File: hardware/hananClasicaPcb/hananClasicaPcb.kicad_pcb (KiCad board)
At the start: 2 copper layers, 77 x 92 mm, 32 parts, among them J1 Jack-DC, J2 Conn_02x04_Top_Bottom, U1 MCP4901

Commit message: hananClasicaPcb v2.0: J2 header -> columna de pads arcade compacta (ODS), gerber regenerado
Co-Authored-By: Claude Fable 5.1 <noreply@anthropic.com>
Claude-Session: https://claude.ai/code/session_018KSRbDX7mTqiibDixEKAXu
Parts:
- J2: value Conn_02x04_Top_Bottom -> Hanan_PadsArcade_1x08_Pares_Compacto; footprint Connector_PinHeader_2.00mm:PinHeader_1x08_P2.00mm_Vertical -> ODS:Hanan_PadsArcade_1x08_Pares_Compacto
- moved J2 10.6 mm to (120.7, 102.0)
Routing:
- net Net-(J2-Pad8): track 153.9 -> 135.8 mm
- net GND: track 440.9 -> 453.4 mm
- net Net-(J2-Pad5): track 144.3 -> 134.6 mm
- net Net-(J2-Pad1): track 136.9 -> 144.1 mm
- net Net-(J2-Pad4): track 128.7 -> 130.8 mm

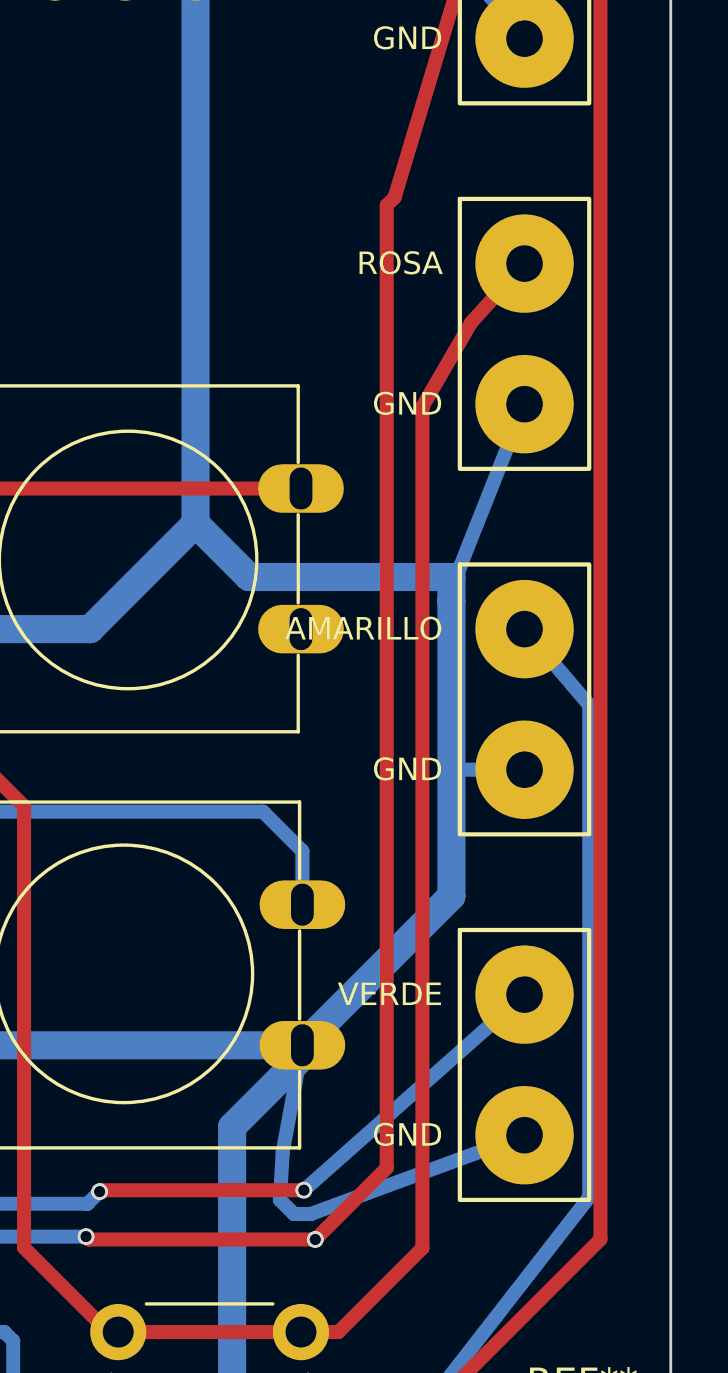
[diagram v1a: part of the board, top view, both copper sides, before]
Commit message: hananClasicaPcb v2.0: columna de pads arcade con grupos espejados; gerber regenerado
Co-Authored-By: Claude Fable 5.1 <noreply@anthropic.com>
Claude-Session: https://claude.ai/code/session_018KSRbDX7mTqiibDixEKAXu
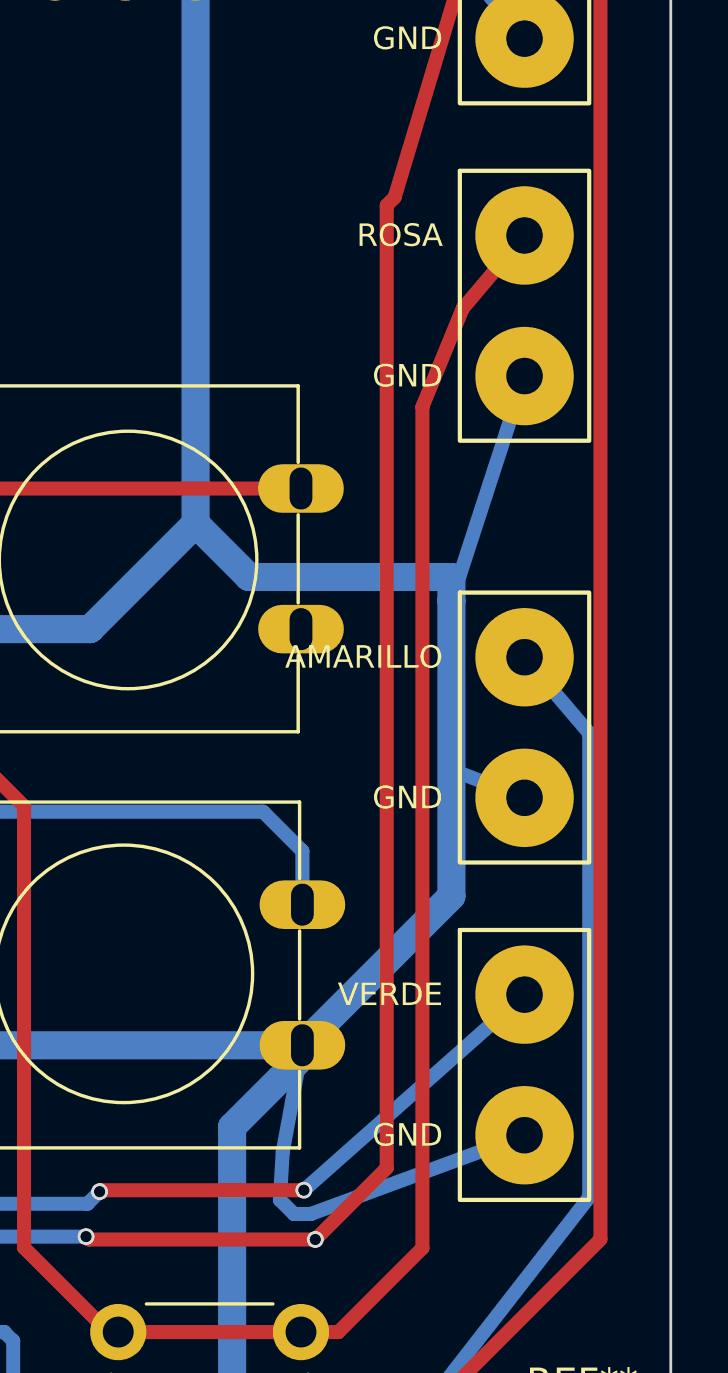
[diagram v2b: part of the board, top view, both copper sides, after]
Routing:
- net GND: track 453.4 -> 454.5 mm
- net Net-(J2-Pad5): track 134.6 -> 133.6 mm
- net Net-(J2-Pad4): track 130.8 -> 131.7 mm
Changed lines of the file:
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@@
 		(layer "F.Cu")
 		(at 120.7 102)
-		(descr "Hanan Cumbia (clasica, version compacta): 8 pads para soldar los cables de los 4 botones arcade, en UNA columna, agrupados de a pares (senal arriba, GND abajo): 5 mm dentro del par; pares 1-2 arriba (paso 17, el LED D1 en el hueco) y pares 3-4 ESPEJADOS respecto del centro de la placa 150x75 (a 4.6 mm de cada borde); offsets 0/5, 13/18, 26/31, 39/44 (version COMPACTA, 44 mm, para la Hanan clasica 77x92 donde la de 66 mm no entra; mismo orden/numeracion/colores). Pad redondo 3.5 mm, agujero 1.3 mm (cable 22 AWG). NUMERACION = pines del simbolo J2 Conn_02x04_Top_Bottom del esquematico hananMiniPcb, en el MISMO orden de colores que el header original: slot1=pad1 (D3, BLANCO/cencerro) slot2=pad2 GND, slot3=pad4 (D8, ROSA/conga) slot4=pad3 GND, slot5=pad5 (D4, AMARILLO/kick) slot6=pad6 GND, slot7=pad8 (D7, VERDE/guiro) slot8=pad7 GND. Colores = botones del panel Mini (manual + firmware hanan26Taller, 2026-10-07). ORIGEN = centro del pad del slot 1 (arriba).")
+		(descr "Hanan Cumbia (clasica, version compacta): 8 pads para soldar los cables de los 4 botones arcade, en UNA columna, agrupados de a pares (senal arriba, GND abajo): 5 mm dentro del par; pares 1-2 arriba (paso 17, el LED D1 en el hueco) y pares 3-4 ESPEJADOS respecto del centro de la placa 150x75 (a 4.6 mm de cada borde); offsets 0/5, 12/17, 27/32, 39/44 (grupos 1-2 y 3-4 ESPEJADOS respecto del centro y=22) (version COMPACTA, 44 mm, para la Hanan clasica 77x92 donde la de 66 mm no entra; mismo orden/numeracion/colores). Pad redondo 3.5 mm, agujero 1.3 mm (cable 22 AWG). NUMERACION = pines del simbolo J2 Conn_02x04_Top_Bottom del esquematico hananMiniPcb, en el MISMO orden de colores que el header original: slot1=pad1 (D3, BLANCO/cencerro) slot2=pad2 GND, slot3=pad4 (D8, ROSA/conga) slot4=pad3 GND, slot5=pad5 (D4, AMARILLO/kick) slot6=pad6 GND, slot7=pad8 (D7, VERDE/guiro) slot8=pad7 GND. Colores = botones del panel Mini (manual + firmware hanan26Taller, 2026-10-07). ORIGEN = centro del pad del slot 1 (arriba).")
 		(tags "hanan arcade solder pads wire pads cable THT 1x08 pares")
 		(property "Reference" "J2"
@@
 		)
 		(fp_rect
-			(start -2.3 10.7)
-			(end 2.3 20.3)
+			(start -2.3 9.7)
+			(end 2.3 19.3)
 			(stroke
 				(width 0.15)
@@
 		)
 		(fp_rect
-			(start -2.3 23.7)
-			(end 2.3 33.3)
+			(start -2.3 24.7)
+			(end 2.3 34.3)
 			(stroke
 				(width 0.15)
@@
 		)
 		(fp_rect
-			(start -2.3 10.7)
-			(end 2.3 20.3)
+			(start -2.3 9.7)
+			(end 2.3 19.3)
 			(stroke
 				(width 0.15)
@@
 		)
 		(fp_rect
-			(start -2.3 23.7)
-			(end 2.3 33.3)
+			(start -2.3 24.7)
+			(end 2.3 34.3)
 			(stroke
 				(width 0.15)
@@
 		)
 		(fp_rect
-			(start -2.5 10.5)
-			(end 2.5 20.5)
+			(start -2.5 9.5)
+			(end 2.5 19.5)
 			(stroke
 				(width 0.05)
@@
 		)
 		(fp_rect
-			(start -2.5 23.5)
-			(end 2.5 33.5)
+			(start -2.5 24.5)
+			(end 2.5 34.5)
 			(stroke
 				(width 0.05)
@@
 		)
 		(fp_rect
-			(start -2.3 10.7)
-			(end 2.3 20.3)
+			(start -2.3 9.7)
+			(end 2.3 19.3)
 			(stroke
 				(width 0.1)
@@
 		)
 		(fp_rect
-			(start -2.3 23.7)
-			(end 2.3 33.3)
+			(start -2.3 24.7)
+			(end 2.3 34.3)
 			(stroke
 				(width 0.1)
@@
 		)
 		(fp_text user "ROSA"
-			(at -2.9 13 0)
+			(at -2.9 12 0)
 			(layer "F.SilkS")
 			(effects
@@
 		)
 		(fp_text user "GND"
-			(at -2.9 18 0)
+			(at -2.9 17 0)
 			(layer "F.SilkS")
 			(effects
@@
 		)
 		(fp_text user "AMARILLO"
-			(at -2.9 26 0)
+			(at -2.9 27 0)
 			(layer "F.SilkS")
 			(effects
@@
 		)
 		(fp_text user "GND"
-			(at -2.9 31 0)
+			(at -2.9 32 0)
 			(layer "F.SilkS")
 			(effects
@@
 		)
 		(fp_text user "ROSA"
-			(at -2.9 13 0)
+			(at -2.9 12 0)
 			(layer "B.SilkS")
 			(effects
@@
 		)
 		(fp_text user "GND"
-			(at -2.9 18 0)
+			(at -2.9 17 0)
 			(layer "B.SilkS")
 			(effects
@@
 		)
 		(fp_text user "AMARILLO"
-			(at -2.9 26 0)
+			(at -2.9 27 0)
 			(layer "B.SilkS")
 			(effects
@@
 		)
 		(fp_text user "GND"
-			(at -2.9 31 0)
+			(at -2.9 32 0)
 			(layer "B.SilkS")
 			(effects
@@
 		)
 		(pad "3" thru_hole circle
-			(at 0 18)
+			(at 0 17)
 			(size 3.5 3.5)
 			(drill 1.3)
@@
 		)
 		(pad "4" thru_hole circle
-			(at 0 13)
+			(at 0 12)
 			(size 3.5 3.5)
 			(drill 1.3)
@@
 		)
 		(pad "5" thru_hole circle
-			(at 0 26)
+			(at 0 27)
 			(size 3.5 3.5)
 			(drill 1.3)
@@
 		)
 		(pad "6" thru_hole circle
-			(at 0 31)
+			(at 0 32)
 			(size 3.5 3.5)
 			(drill 1.3)
@@
 	)
 	(segment
-		(start 118.4 99.7)
-		(end 119.2 98.9)
-		(width 0.5)
-		(layer "B.Cu")
-		(net "GND")
-	)
-	(segment
-		(start 118.1 126.146)
-		(end 118.1 127)
-		(width 1)
-		(layer "B.Cu")
-		(net "GND")
-	)
-	(segment
 		(start 112.8 142.8)
 		(end 112.8 143.2)
@@
 	)
 	(segment
-		(start 118.4 125.8)
-		(end 118.1 127)
-		(width 0.5)
-		(layer "B.Cu")
-		(net "GND")
-	)
-	(segment
 		(start 54.9 122)
 		(end 57.5 122)
@@
 	)
 	(segment
-		(start 120.7 120)
-		(end 118.4 125.8)
-		(width 0.5)
-		(layer "B.Cu")
-		(net "GND")
-	)
-	(segment
 		(start 72.6 81.4976)
 		(end 72.6 83.6)
@@
 	)
 	(segment
+		(start 112.5 148.8)
+		(end 112 148.3)
+		(width 0.5)
+		(layer "B.Cu")
+		(net "GND")
+	)
+	(segment
 		(start 109 124.25)
 		(end 110.8964 126.1464)
@@
 	)
 	(segment
-		(start 112 148.3)
-		(end 112.1 146.6)
-		(width 0.5)
-		(layer "B.Cu")
-		(net "GND")
-	)
-	(segment
 		(start 53.6 105.8)
 		(end 60.3 110.7)
@@
 	)
 	(segment
-		(start 112.1 146.6)
-		(end 112.8 142.8)
+		(start 118.4 99.7)
+		(end 119.2 98.9)
 		(width 0.5)
 		(layer "B.Cu")
@@
 	)
 	(segment
-		(start 120.7 146)
-		(end 113.1 148.8)
+		(start 112.1 146.6)
+		(end 112.8 142.8)
 		(width 0.5)
 		(layer "B.Cu")
@@
 	)
 	(segment
-		(start 118.1 127)
-		(end 118.1 137.5)
-		(width 1)
+		(start 112 148.3)
+		(end 112.1 146.6)
+		(width 0.5)
 		(layer "B.Cu")
 		(net "GND")
@@
 	)
 	(segment
-		(start 120.7 107)
-		(end 118.4 104.2)
-		(width 0.5)
-		(layer "B.Cu")
-		(net "GND")
-	)
-	(segment
-		(start 118.4 104.2)
-		(end 118.4 99.7)
+		(start 113.1 148.8)
+		(end 112.5 148.8)
 		(width 0.5)
 		(layer "B.Cu")
@@
 	)
 	(segment
+		(start 120.7 119)
+		(end 118.1 127)
+		(width 0.5)
+		(layer "B.Cu")
+		(net "GND")
+	)
+	(segment
 		(start 64.78 111.24)
 		(end 65.36 111.24)
@@
 	)
 	(segment
+		(start 120.7 146)
+		(end 113.1 148.8)
+		(width 0.5)
+		(layer "B.Cu")
+		(net "GND")
+	)
+	(segment
 		(start 62.25 157.5)
 		(end 60 157.5)
@@
 	)
 	(segment
+		(start 118.1 127)
+		(end 118.1 137.5)
+		(width 1)
+		(layer "B.Cu")
+		(net "GND")
+	)
+	(segment
 		(start 110.8964 126.1464)
 		(end 118.1 126.1464)
@@
 	)
 	(segment
-		(start 113.1 148.8)
-		(end 112.5 148.8)
+		(start 118.4 104.2)
+		(end 118.4 99.7)
 		(width 0.5)
 		(layer "B.Cu")
@@
 	)
 	(segment
-		(start 112.5 148.8)
-		(end 112 148.3)
+		(start 118.1 126.15)
+		(end 118.1 127)
+		(width 1)
+		(layer "B.Cu")
+		(net "GND")
+	)
+	(segment
+		(start 120.7 107)
+		(end 118.4 104.2)
 		(width 0.5)
 		(layer "B.Cu")
@@
 	)
 	(segment
-		(start 120.7 133)
+		(start 120.7 134)
 		(end 118.1 133)
 		(width 0.5)
@@
 	)
 	(segment
-		(start 77.25 153)
-		(end 77.25 101.25)
+		(start 116.078 112.649)
+		(end 118.5 104.6)
 		(width 0.5)
 		(layer "F.Cu")
@@
 	)
 	(segment
-		(start 105.2068 149.7076)
-		(end 105.1052 149.606)
+		(start 77.25 153)
+		(end 77.25 101.25)
 		(width 0.5)
 		(layer "F.Cu")
@@
 	)
 	(segment
-		(start 118.5 104.6)
-		(end 120.7 102)
+		(start 105.2068 149.7076)
+		(end 105.1052 149.606)
 		(width 0.5)
 		(layer "F.Cu")
@@
 	(segment
 		(start 116.078 112.649)
-		(end 118.5 104.6)
+		(end 115.7986 112.9284)
 		(width 0.5)
 		(layer "F.Cu")
@@
 	)
 	(segment
-		(start 116.078 112.649)
-		(end 115.7986 112.9284)
+		(start 118.5 104.6)
+		(end 120.7 102)
 		(width 0.5)
 		(layer "F.Cu")
@@
 	(segment
 		(start 112.395 161.8234)
+		(end 123 148.2)
+		(width 0.5)
+		(layer "B.Cu")
+		(net "Net-(J2-Pad5)")
+	)
+	(segment
+		(start 112.395 161.8234)
 		(end 103.6828 161.8234)
 		(width 0.5)
@@
 	(segment
 		(start 123 148.2)
-		(end 123 130.7)
+		(end 123 131.7)
 		(width 0.5)
 		(layer "B.Cu")
@@
 	)
 	(segment
-		(start 112.395 161.8234)
-		(end 123 148.2)
-		(width 0.5)
-		(layer "B.Cu")
-		(net "Net-(J2-Pad5)")
-	)
-	(segment
-		(start 123 130.7)
-		(end 120.7 128)
+		(start 123 131.7)
+		(end 120.7 129)
 		(width 0.5)
 		(layer "B.Cu")
@@
 	)
 	(segment
-		(start 118.8 117.1)
-		(end 120.7 115)
+		(start 106.25 153)
+		(end 112.75 153)
 		(width 0.5)
 		(layer "F.Cu")
@@
 	)
 	(segment
-		(start 106.25 153)
-		(end 112.75 153)
+		(start 117.0686 120.0912)
+		(end 118.5 116.6)
 		(width 0.5)
 		(layer "F.Cu")
@@
 	)
 	(segment
-		(start 117.0686 120.0912)
-		(end 118.8 117.1)
+		(start 118.5 116.6)
+		(end 120.7 114)
 		(width 0.5)
 		(layer "F.Cu")
